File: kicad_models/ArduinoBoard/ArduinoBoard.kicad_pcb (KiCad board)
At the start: 2 copper layers, 214.8 x 70 mm, 44 parts, among them J1 5V Output, J10 Conn_01x06_Pin, J11 Conn_02x04_Odd_Even, J12 Conn_01x01, J13 Conn_01x01, J2 Buttons, J3 PWM Output, J4 12V Input, J5 Conn_01x04_Pin, J6 Conn_01x04_Pin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

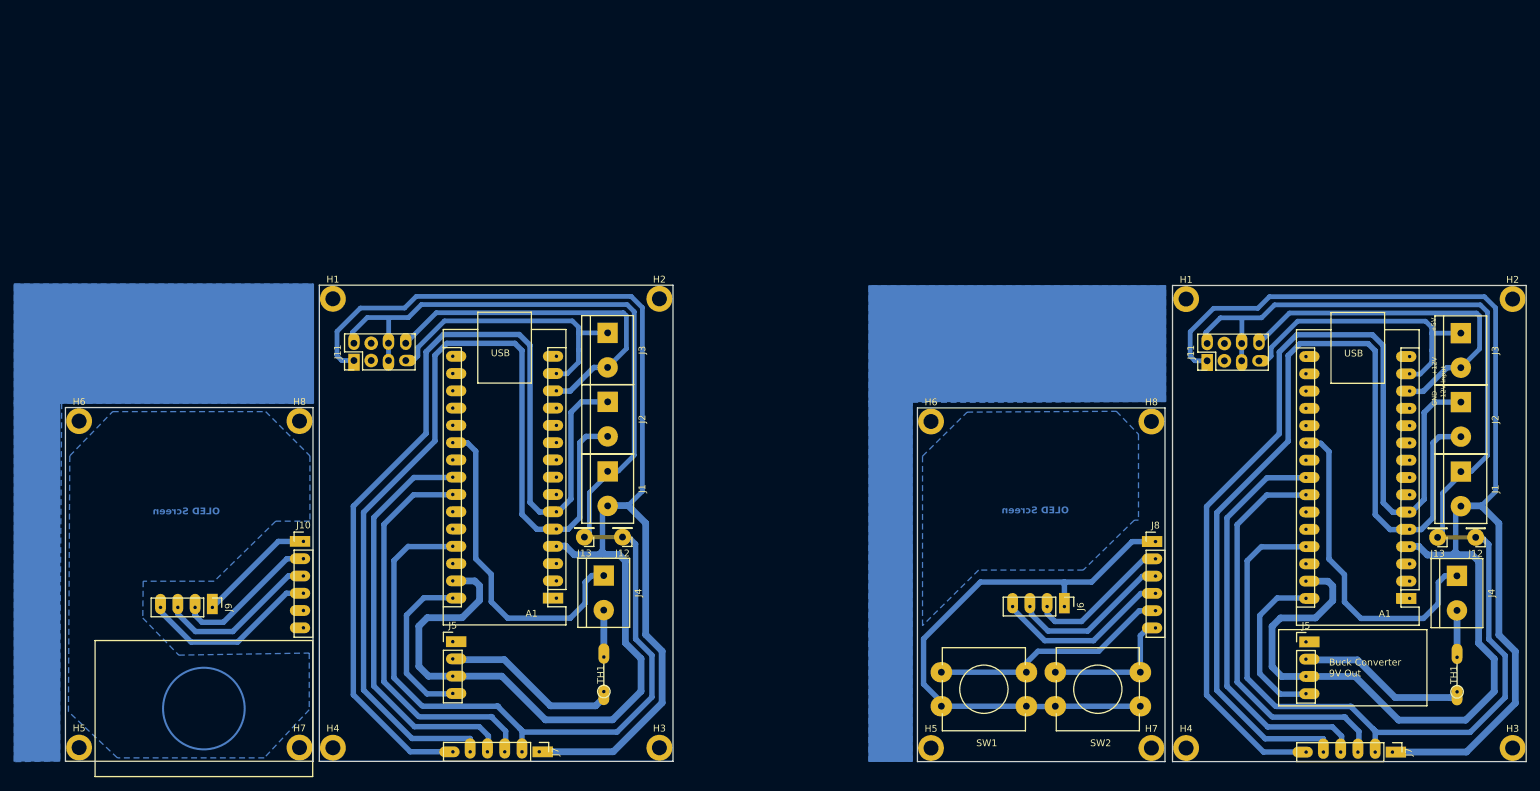
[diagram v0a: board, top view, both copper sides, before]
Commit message: Redesigned the PCB - moved the screw terminals for the switch to the other side of the board and changed to analog GPIO (A2 & A3) rather than Digital. Moved the two screw holes that were toward the front of the gauge back about 10mm to give it some space for brass inserts. Updated the Arduino code to use the new GPIO for the switch actuation. Also updated the Solid Edge/STL files to match the new screw holes in the PCB.
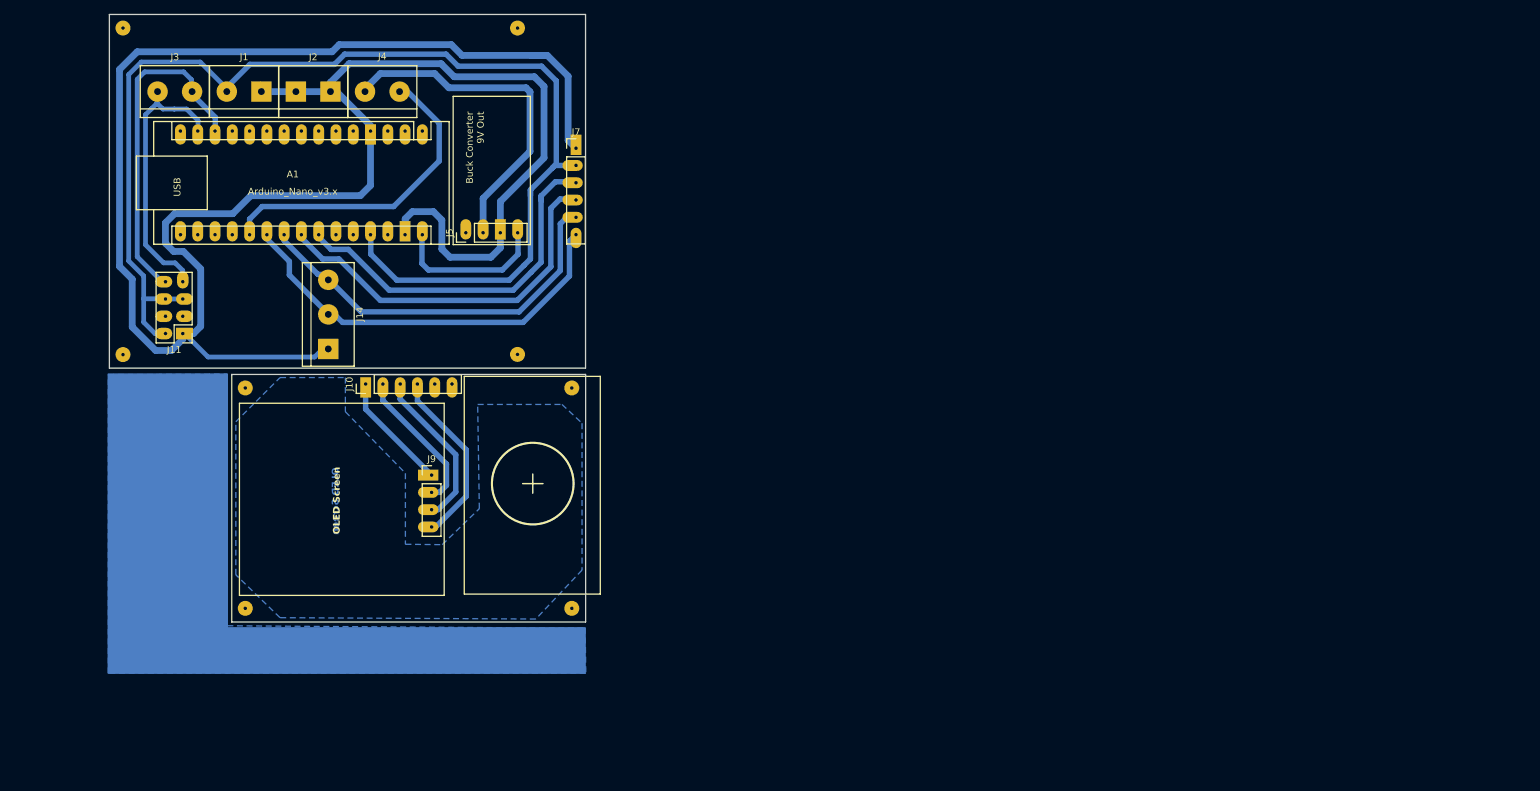
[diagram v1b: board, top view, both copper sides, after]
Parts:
- removed the A1 at (230.5, 125.8)
- removed the H1 at (197.6, 81.8)
- removed the H2 at (245.6, 81.8)
- removed the H3 at (245.6, 147.8)
- removed the H4 at (197.6, 147.8)
- removed the H5 at (160.1, 147.8)
- removed the H6 at (160.1, 99.8)
- removed the H7 at (192.5, 147.8)
- removed the H8 at (192.5, 99.8)
- removed the J1 at (238.0, 107.2)
- removed the J11 at (200.7, 90.9)
- removed J12 (x2), J13 (x2): Conn_01x01, Connector_PinHeader_2.54mm:PinHeader_1x01_P2.54mm_Vertical
- removed the J2 at (112.6, 96.9)
- removed the J2 at (238.0, 97.0)
- removed the J3 at (238.0, 86.8)
- removed the J4 at (237.4, 122.5)
- removed the J5 at (215.2, 132.2)
- removed J6: Conn_01x04_Pin, Connector_PinHeader_2.54mm:PinHeader_1x04_P2.54mm_Vertical
- removed the J7 at (227.9, 148.4)
- removed J8: Conn_01x06_Pin, Connector_PinHeader_2.54mm:PinHeader_1x06_P2.54mm_Vertical
- removed SW1, SW2: SW_Push_Dual, Button_Switch_THT:SW_PUSH-12mm
- removed TH1 (x2): Thermistor_NTC, Resistor_THT:R_Axial_DIN0204_L3.6mm_D1.6mm_P5.08mm_Vertical
- added J14: Switch/Buttons, TerminalBlock:TerminalBlock_bornier-3_P5.08mm, F.Cu at (71.5, 79.0)
- added J2: 5V Output, TerminalBlock:TerminalBlock_bornier-2_P5.08mm, F.Cu at (66.7, 51.3)
- moved H3 107.8 mm to (99.3, 42.0), turned to 90 degrees
- moved J7 88.9 mm to (107.9, 59.6), turned to 0 degrees
- moved H2 88.3 mm to (41.3, 42.0), turned to 90 degrees
- moved J4 79.3 mm to (76.9, 51.3), turned to 0 degrees
- moved J1 79.1 mm to (56.6, 51.3), turned to 0 degrees
- moved H5 75.3 mm to (107.3, 127.3), turned to 90 degrees
- moved J3 75.1 mm to (46.4, 51.3), turned to 0 degrees
- moved A1 71.4 mm to (85.3, 57.1), turned to -90 degrees
- moved H7 66.3 mm to (107.3, 94.9), turned to 90 degrees
- moved H4 63.9 mm to (99.3, 90.0), turned to 90 degrees
- moved J5 60.1 mm to (91.7, 72.1), turned to 90 degrees
- moved J9 37.6 mm to (86.7, 107.7), turned to 0 degrees
- moved H6 36.8 mm to (59.3, 127.3), turned to 90 degrees
- moved H1 31.9 mm to (41.3, 90.0), turned to 90 degrees
- moved J11 25.5 mm to (50.1, 86.9), turned to 180 degrees
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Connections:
- A1 pad 20: unconnected-(A1-A1-Pad20) -> Net-(A1-A1)
- A1 pad 22: unconnected-(A1-A3-Pad22) -> Net-(A1-A3)
- A1 pad 5: Net-(A1-D2) -> unconnected-(A1-D2-Pad5)
- A1 pad 6: Net-(A1-D3) -> unconnected-(A1-D3-Pad6)
- J4 pad 1: Net-(A1-A2) -> /VI+
- J4 pad 2: Net-(J4-Pin_2) -> Net-(A1-A1)
- J7 pad 5: Net-(A1-D2) -> Net-(A1-A3)
- J7 pad 6: Net-(A1-D3) -> Net-(A1-A2)
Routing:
- net Net-(A1-D3): track 277.3 -> 0.00 mm
- net Net-(A1-D2): track 274.6 -> 0.00 mm
- net Net-(A1-+5V): track 383.8 -> 178.8 mm
- net /GND: track 477.3 -> 320.6 mm
- net Net-(J6-Pin_1): track 82.6 -> 0.00 mm
- net Net-(A1-A4): track 121.1 -> 55.3 mm
- net Net-(A1-A5): track 117.1 -> 54.0 mm
- net Net-(A1-A3): track 0.00 -> 58.3 mm
- net Net-(A1-D10): track 103.0 -> 51.1 mm
- net Net-(A1-A1): track 0.00 -> 47.3 mm
- net Net-(A1-D11): track 81.9 -> 41.1 mm
- net Net-(A1-A2): track 97.7 -> 60.7 mm
- net Net-(J8-Pin_5): track 35.2 -> 0.00 mm
- net Net-(J6-Pin_4): track 26.0 -> 0.00 mm
- net /VO+: track 48.7 -> 22.8 mm
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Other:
- board size 214.8 x 70 mm -> 70 x 89.3 mm
- board text added: "+12V INPUT"
- board text added: "+5V OUT"
- board text added: "EXT"
- board text added: "EXT RET"
- board text added: "MOTOR CTLR"
- board text added: "POSITION SENSOR"
- board text added: "Position Sensor"
- board text added: "RET"
- board text added: "SWITCH/BUTTONS"
- board text removed: "+12V"
- board text removed: "12V Input"
- board text removed: "5V Power"
- board text removed: "Buttons"
- board text removed: "Ext Ret"
- board text removed: "Pos. Sensor"
- board text removed: "SW2"
- board text removed: "TH1 NTC Thermistor"
- board text removed: "TO MOTOR CONTROLLER"

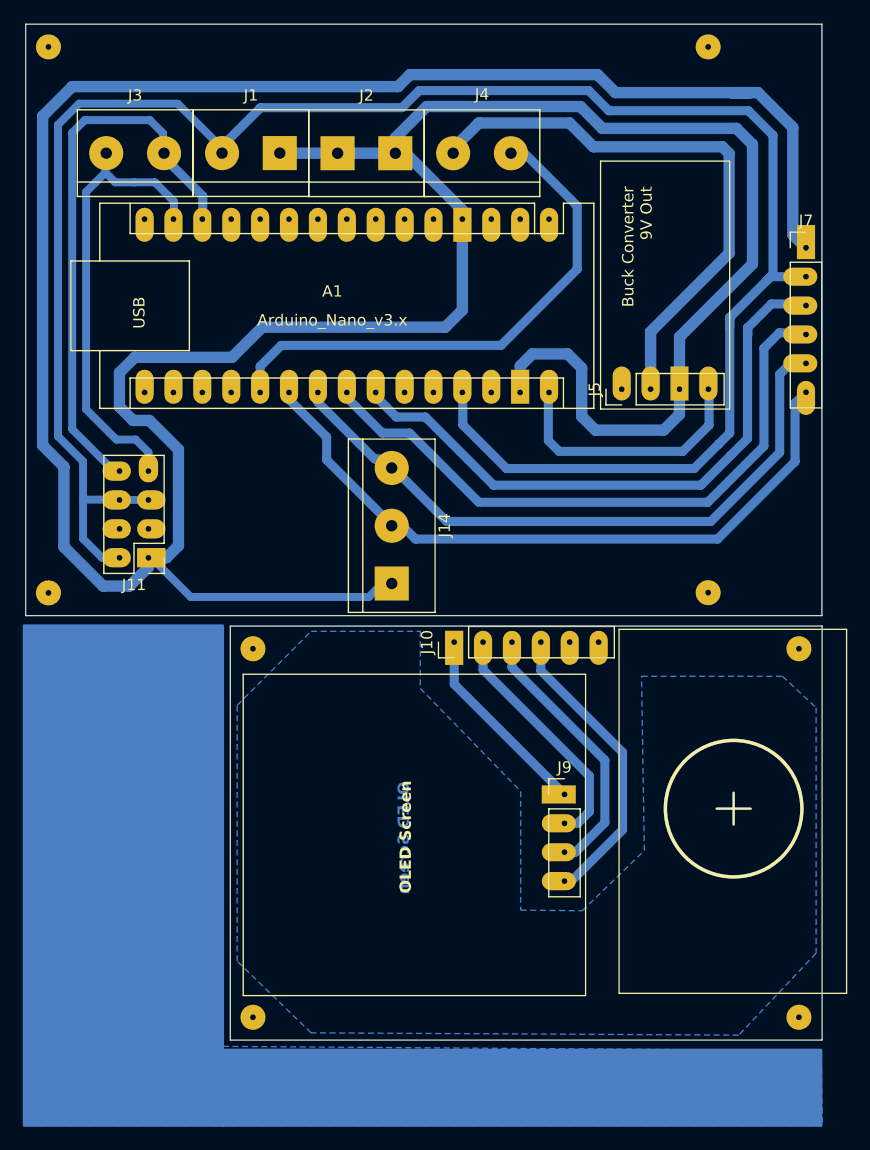
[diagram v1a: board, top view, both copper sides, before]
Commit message: Updated the code a little, but mostly added Gerber files that can be used to purchase custom PCBs from one of the many PCB manufacturing companies.
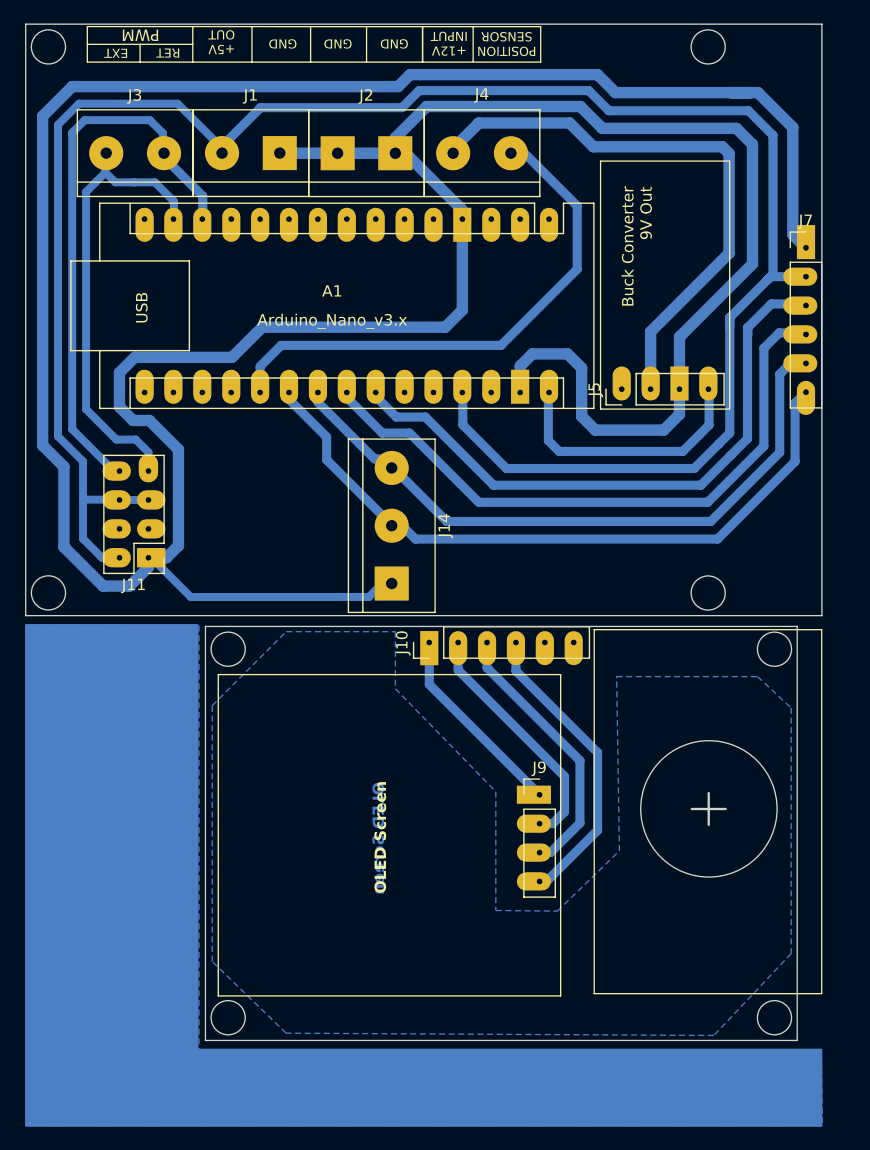
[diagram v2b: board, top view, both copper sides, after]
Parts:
- removed H1, H2, H3, H4, H5, H6, H7, H8: MountingHole, MountingHole:MountingHole_2.2mm_M2_DIN965_Pad
- moved J9 2.19 mm to (84.5, 107.7)
- moved J10 2.19 mm to (74.8, 94.3)
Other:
- outline, holes or cut-outs redrawn

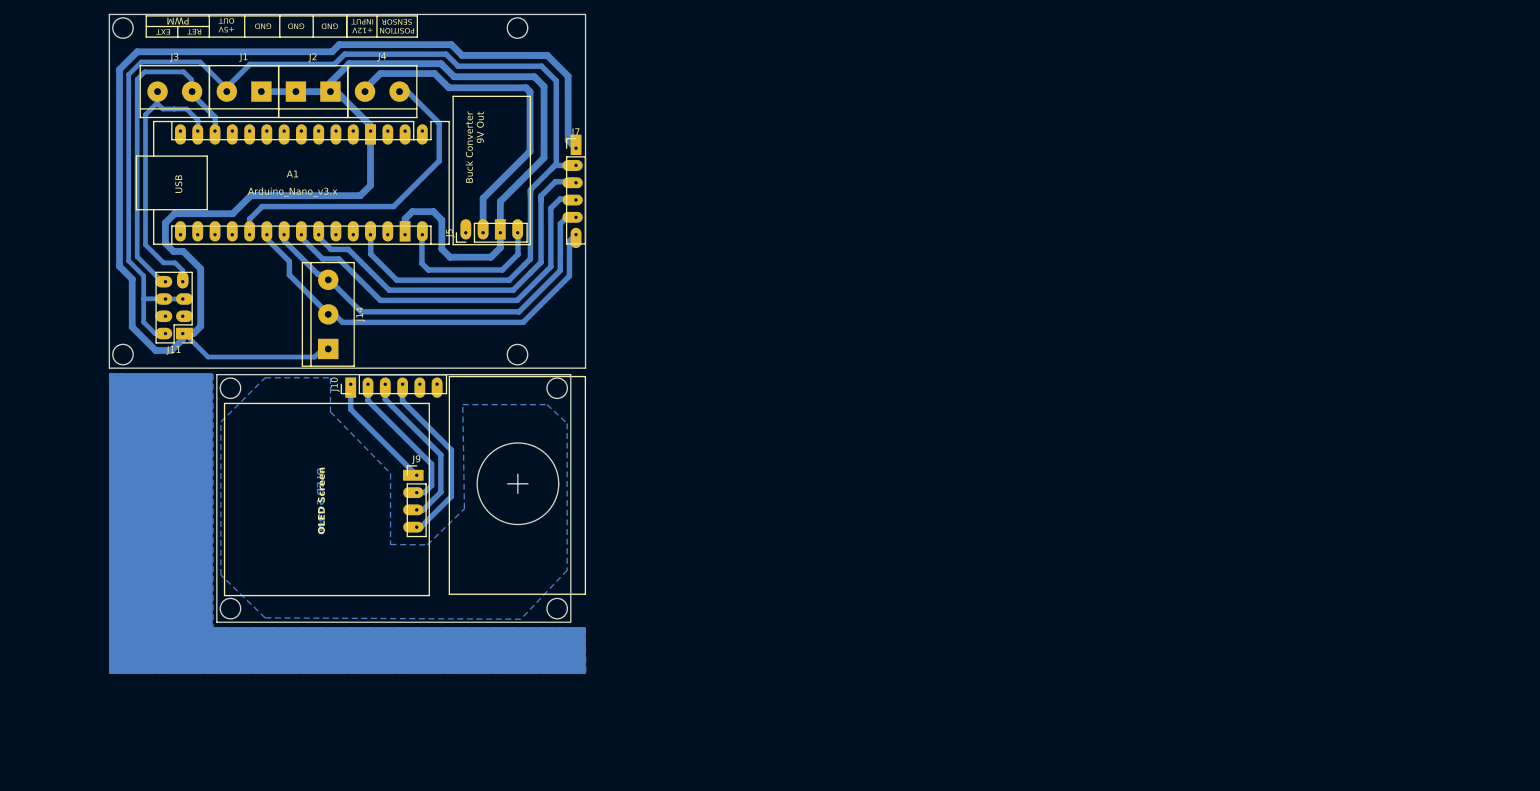
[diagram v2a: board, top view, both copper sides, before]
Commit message: Fixed a gerber file issue reported by Jon Parnaby. He noted that a lot of the through holes in the PCBs he ordered from JLCPCB were too small (for Arduino and other components). I grew the holes from .5mm to 1.0mm. I also split the PCB into two separate projects so that it would be easier to send them off to be manufactured.
Also updated the printable PDFs for PCB transfer paper (e.g. reversed, underside, copper-only).
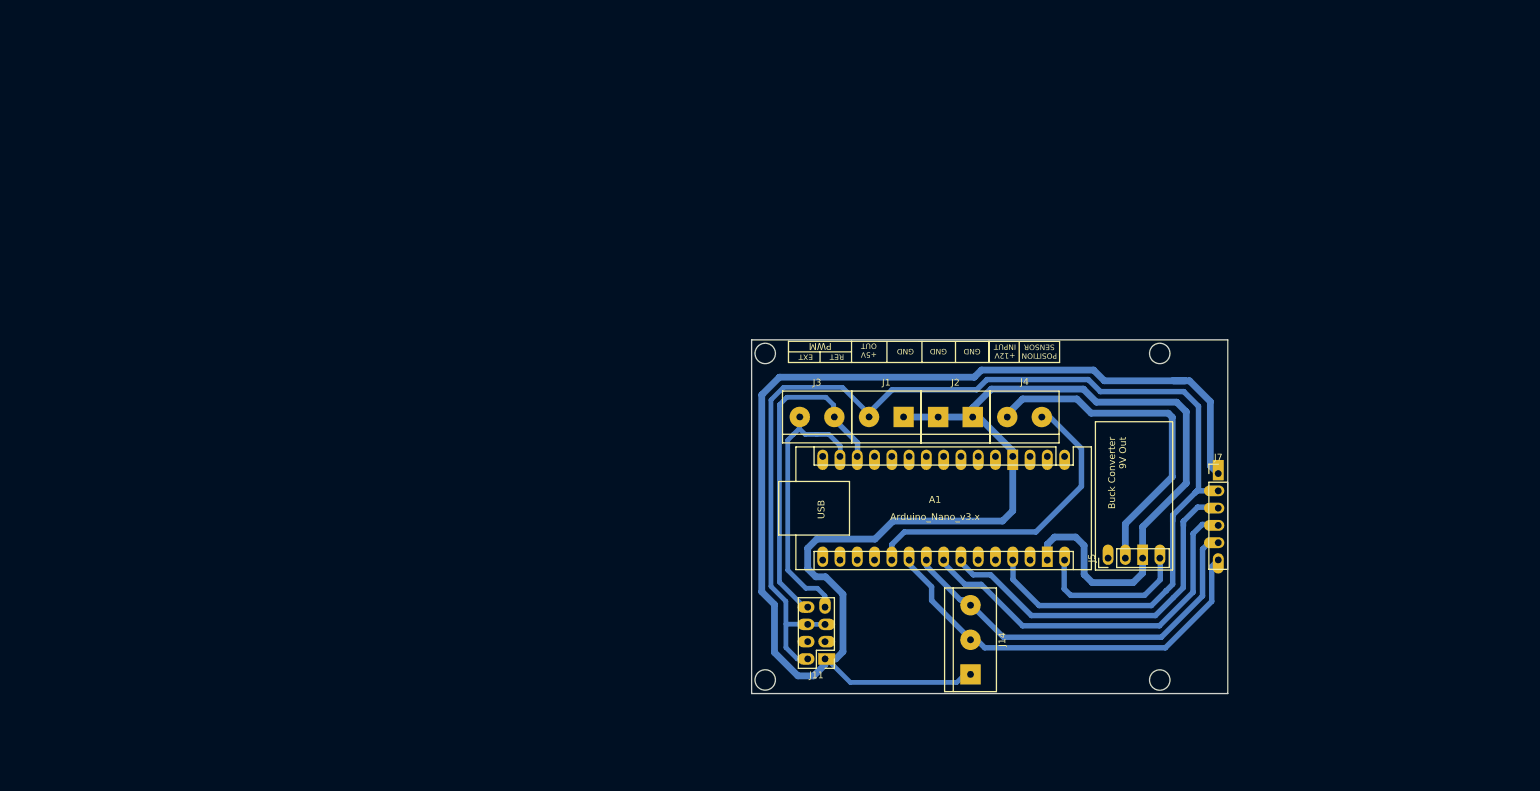
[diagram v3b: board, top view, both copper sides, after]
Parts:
- removed J10: Conn_01x06_Pin, Connector_PinHeader_2.54mm:PinHeader_1x06_P2.54mm_Vertical
- removed J9: Conn_01x04_Pin, Connector_PinHeader_2.54mm:PinHeader_1x04_P2.54mm_Vertical
- moved A1 105.8 mm to (179.7, 104.9)
- moved J1 105.8 mm to (151.0, 99.1)
- moved J2 105.8 mm to (161.1, 99.1)
- moved J3 105.8 mm to (140.8, 99.1)
- moved J4 105.8 mm to (171.3, 99.1)
- moved J5 105.8 mm to (186.1, 119.9)
- moved J11 105.8 mm to (144.5, 134.7)
- moved J14 105.8 mm to (165.9, 126.8)
- moved J7 105.8 mm to (202.3, 107.5)
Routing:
- net Net-(J10-Pin_4): track 26.4 -> 0.00 mm
- net Net-(J10-Pin_3): track 23.9 -> 0.00 mm
- net Net-(J10-Pin_2): track 21.4 -> 0.00 mm
- net Net-(J10-Pin_1): track 17.4 -> 0.00 mm
- removed copper zone on B.Cu, net (none)
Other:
- board size 70 x 89.3 mm -> 70 x 52 mm
- board text removed: "90 deg male pins"
- board text removed: "OLED Screen"
- board text removed: "Position Sensor"
- board text removed: "SW1"
